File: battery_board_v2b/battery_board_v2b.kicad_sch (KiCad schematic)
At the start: 117 parts, among them IC1 PCA9685PW,118, IC2 LT3652IMSE#PBF, IC3 PCT2075DP,118, J1 Face0, J11 CHARGE, J12 Foot0, J13 Foot1, J14 Foot2, J15 Foot3, J16 RBF, J17 BURN, J18 Bypass, J19 Heater, J2 Face1, J3 Face2, J4 Face3, J5 Face4, J6 FC_FACE, J7 5V Breakout, J8 ISS Foot, K1 APAN3105, Q1 IRF7458, Q2 IRF7458, Q3 MBT2222ADW1T1, Q4 MBT2222ADW1T1, Q5 IRLML2803, Q6 NDS8434, Q7 MMBT2222AT, Q8 IRLML2803, Q9 NDS8434, U1 R5460N208AA, U2 TPS54226PWPRPWP14_2P31X2P46-L, U3 INA219AxD, U4 TCA9548APWR, U5 TPS7A4501DCQT, U6 INA219AxD, U7 1049, U8 1049

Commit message: Updated to add thermocouple driver onboard
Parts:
- added C21, C23: 0.01uF, Capacitor_SMD:C_0805_2012Metric, symbol Device:C
- added C22, C27: 0.1uF, Capacitor_SMD:C_0805_2012Metric, symbol Device:C
- added C24: 1uF, Capacitor_SMD:C_0805_2012Metric, symbol Device:C
- added C25, C26: 10uF, Capacitor_SMD:C_0805_2012Metric, symbol Device:C
- added FB1, FB2, FB3: FerriteBead, Resistor_SMD:R_0603_1608Metric, symbol Device:FerriteBead
- added J9: Thermocouple, MOLEX PICO LOCK 2 POS:MOLEX_504050-0291, symbol Connector_Generic:Conn_01x02
- added JP2: SolderJumper_2_Open, Jumper:SolderJumper-2_P1.3mm_Open_RoundedPad1.0x1.5mm, symbol Jumper:SolderJumper_2_Open
- added R46: 1-MOhm, Resistor_SMD:R_0603_1608Metric, symbol Device:R_US
- added R47, R48: 100-Ohm, Resistor_SMD:R_0603_1608Metric, symbol Device:R_US
- added R49: 1k, Resistor_SMD:R_0603_1608Metric, symbol Device:R_US
- added R50: 10k-Ohm, Resistor_SMD:R_0603_1608Metric, symbol Device:R_US
- added U10: TLVH431 DBZ SOT-23, Package_TO_SOT_SMD:SOT-23, symbol Reference_Voltage:TL431DBZ
- added U11: ADS1015IDGS, Package_SO:TSSOP-10_3x3mm_P0.5mm, symbol Analog_ADC:ADS1015IDGS
- added U9: AD8495, Package_SO:MSOP-8_3x3mm_P0.65mm, symbol Sensor_Temperature:AD8495
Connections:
- net +3V3: now also C26.2, FB1.2, FB2.2, JP2.2 (B)
- net F4_SCL: now also U11.10 (SCL)
- net F4_SDA: now also U11.9 (SDA)
- net GND: now also C21.1, C23.2, C24.2, C26.1, FB3.2, R46.2, R50.1, U10.3 (A), U9.3 (-Vs)
- new net: JP2.1 (A), R50.2, U11.1 (ADDR)
- new net: J9.1 (Pin_1), R46.1, R48.2
- new net: C24.1, FB1.1, R49.2, U9.7 (+Vs)
- new net: C21.2, C22.2, R47.2, U9.1 (-IN)
- new net: C22.1, C23.1, R48.1, U9.8 (+IN)
- new net: J9.2 (Pin_2), R47.1
- new net: R49.1, U10.1 (K), U10.2 (REF), U9.2 (REF)
- new net AGND: C25.2, C27.2, FB3.1, U11.3 (GND)
- new net AVDD: C25.1, C27.1, FB2.1, U11.4 (AIN0), U11.6 (AIN2), U11.7 (AIN3), U11.8 (VDD)
- new net OUT: U11.5 (AIN1), U9.5 (SENSE), U9.6
- no-connect marks 26 -> 27
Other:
- note added: "Default I2C: 0x48"
- note added: "Jumped I2C: 0x49"
- moved on the sheet: J11, J17, J18, J19, J5, J6, J7, J8, R45

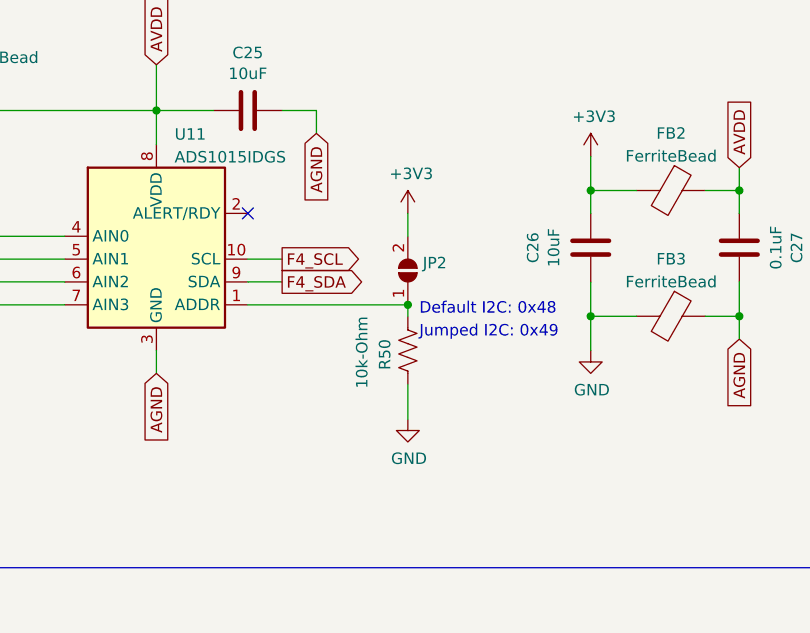
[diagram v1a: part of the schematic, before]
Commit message: Placed the thermocoupler circuitry on the board and modified schematic FOr the schematic I removed the adresse jumper ase we know which I2C adresse we are using.
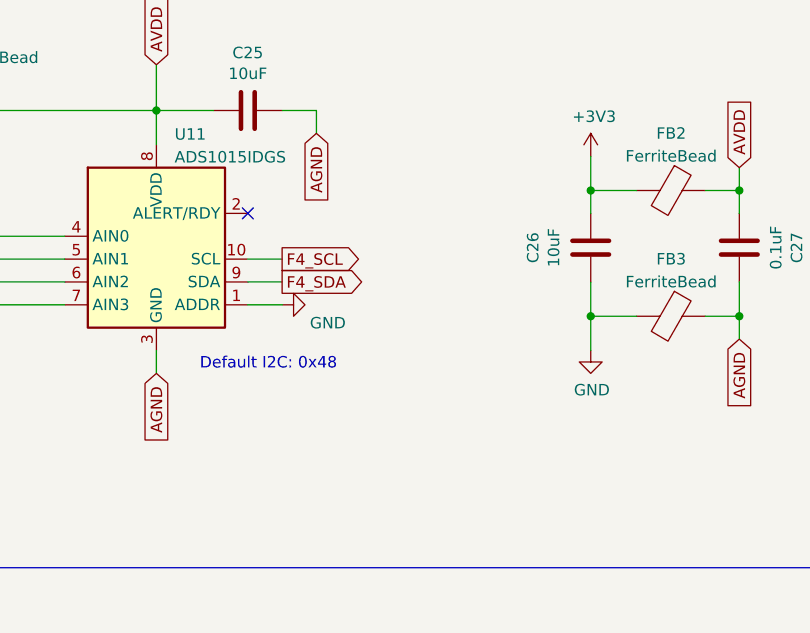
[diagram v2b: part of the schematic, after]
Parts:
- removed JP2: SolderJumper_2_Open, Jumper:SolderJumper-2_P1.3mm_Open_RoundedPad1.0x1.5mm, symbol Jumper:SolderJumper_2_Open
- removed R50: 10k-Ohm, Resistor_SMD:R_0603_1608Metric, symbol Device:R_US
- C21, C22, C23, C24, C25, C26, C27: footprint Capacitor_SMD:C_0805_2012Metric -> Capacitor_SMD:C_0402_1005Metric_Pad0.74x0.62mm_HandSolder
- R46, R47, R48, R49: footprint Resistor_SMD:R_0603_1608Metric -> Resistor_SMD:R_0402_1005Metric_Pad0.72x0.64mm_HandSolder
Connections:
- net GND: now also U11.1 (ADDR)
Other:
- note removed: "Jumped I2C: 0x49"

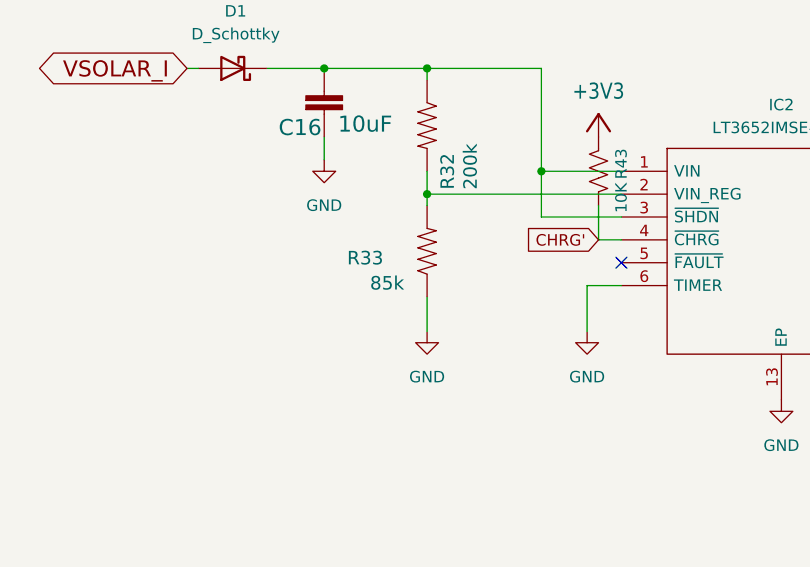
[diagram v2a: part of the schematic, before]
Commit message: Updated BOM to reflect parts availability
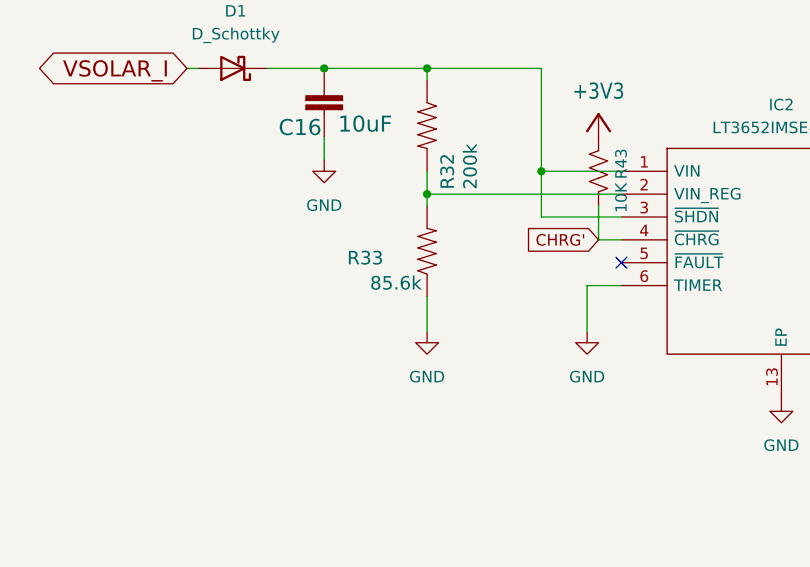
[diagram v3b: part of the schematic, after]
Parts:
- R33: value 85k -> 85.6k
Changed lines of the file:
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@@
 			)
 		)
-		(property "Value" "85k"
+		(property "Value" "85.6k"
 			(at 452.12 147.066 90)
 			(effects

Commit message: Reliability Improvements
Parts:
- removed C13, C19: 200uF, Capacitor_SMD:C_1210_3225Metric, symbol Device:C
- removed R45: 0.002, Resistor_SMD:R_2512_6332Metric, symbol mainboard:R-US_R2512
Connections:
- net B-: now also J8.2 (Pin_2)
- net GND: no longer J8.2 (Pin_2)

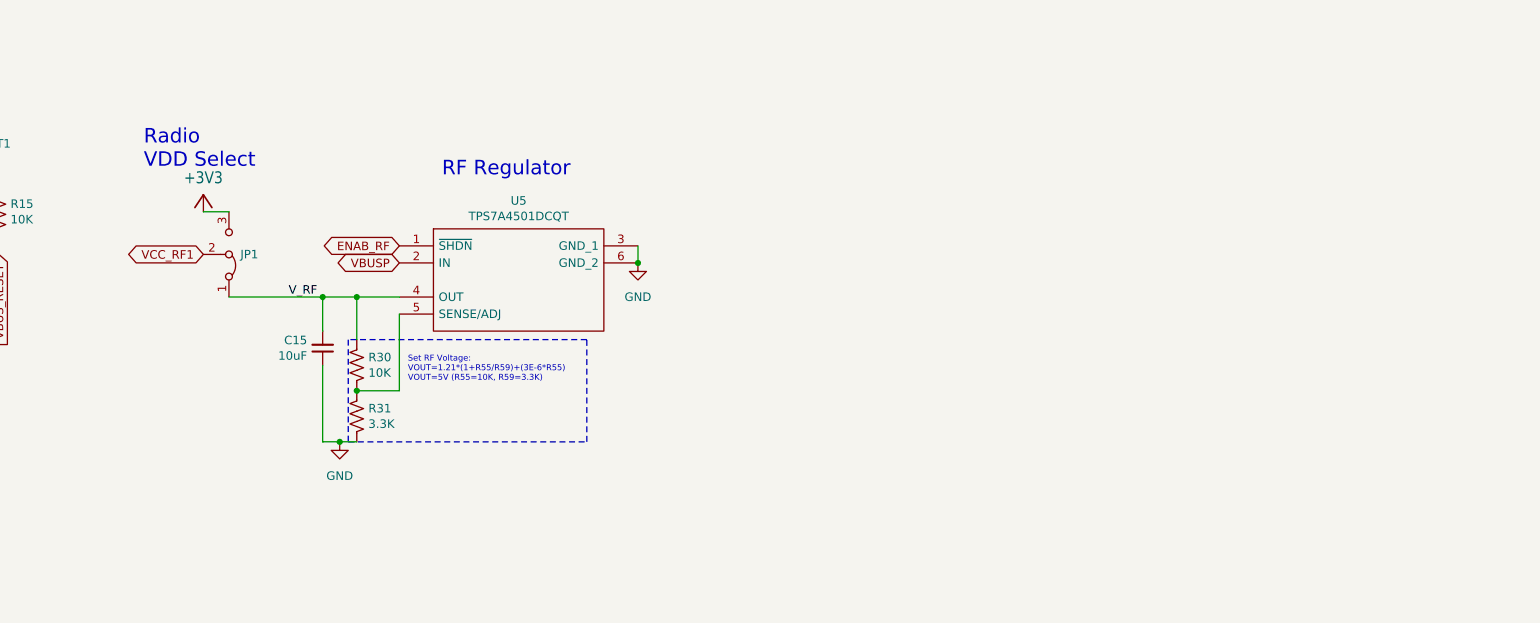
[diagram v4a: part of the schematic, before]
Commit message: Changed the 5V buck converter to a more efficient one
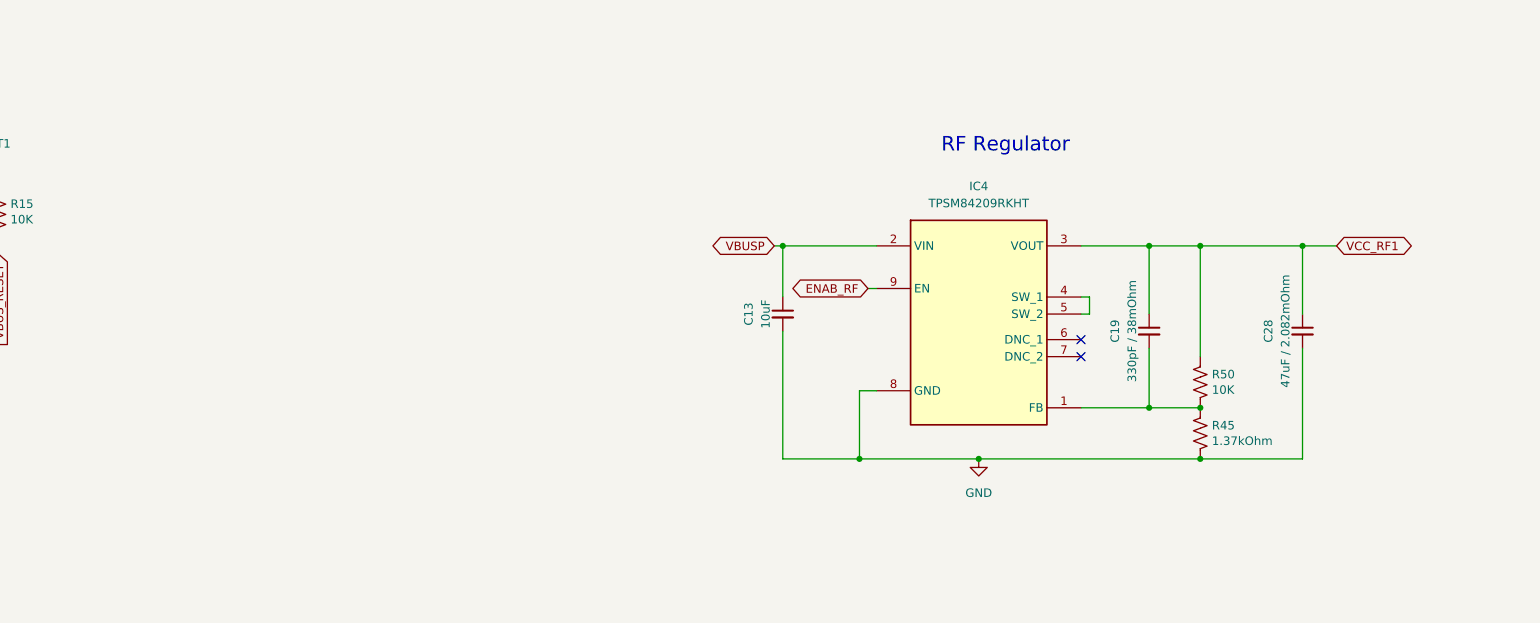
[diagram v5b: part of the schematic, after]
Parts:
- removed C15: 10uF, Capacitor_SMD:C_0603_1608Metric, symbol Device:C_Small
- removed JP1: Jumper_3_Bridged12, MaxLib:SolderJumper-3_P1.3mm_Bridged12_RoundedPad1.0x1.5mm, symbol mainboard-rescue:Jumper_3_Bridged12-Jumper
- removed R30: 10K, Resistor_SMD:R_0603_1608Metric, symbol Device:R_US
- removed R31: 3.3K, Resistor_SMD:R_0603_1608Metric, symbol Device:R_US
- removed U5: TPS7A4501DCQT, MaxLib:TPS7A4501DCQT, symbol mainboard:TPS7A4501DCQT
- added C13: 10uF, Capacitor_SMD:C_0603_1608Metric, symbol Device:C_Small
- added C19: 330pF / 38mOhm, Capacitor_SMD:C_0603_1608Metric, symbol Device:C_Small
- added C28: 47uF / 2.082mOhm, Capacitor_SMD:C_0603_1608Metric, symbol Device:C_Small
- added IC4: TPSM84209RKHT, TPSM84209RKHT, symbol Battery_Board:TPSM84209RKHT
- added R45: 1.37kOhm, Resistor_SMD:R_0603_1608Metric, symbol Device:R_US
- added R50: 10K, Resistor_SMD:R_0603_1608Metric, symbol Device:R_US
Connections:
- net ENAB_RF: now also IC4.9 (EN)
- net GND: now also C13.2, C28.2, IC4.8 (GND), R45.2
- net VBUSP: now also C13.1, IC4.2 (VIN)
- net VCC_RF1: now also C19.1, C28.1, IC4.3 (VOUT), R50.1
- new net: C19.2, IC4.1 (FB), R45.1, R50.2
- new net: IC4.4 (SW_1), IC4.5 (SW_2)
- no-connect marks 27 -> 29
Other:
- note removed: "Radio VDD Select"
- note removed: "Set RF Voltage: VOUT=1.21*(1+R55/R59)+(3E-6*R55) VOUT=5V (R55=10K, R59=3.3K)"

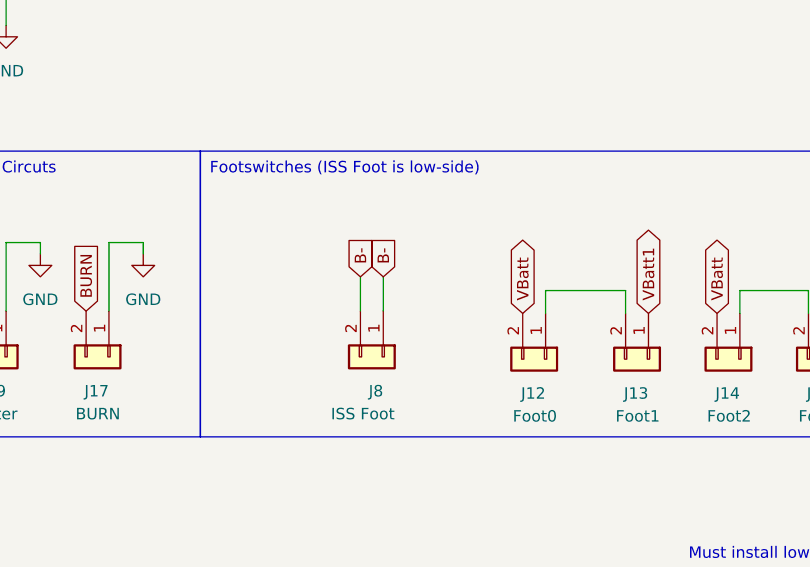
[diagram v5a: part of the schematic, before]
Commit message: Updated 5v reg and lowside switch
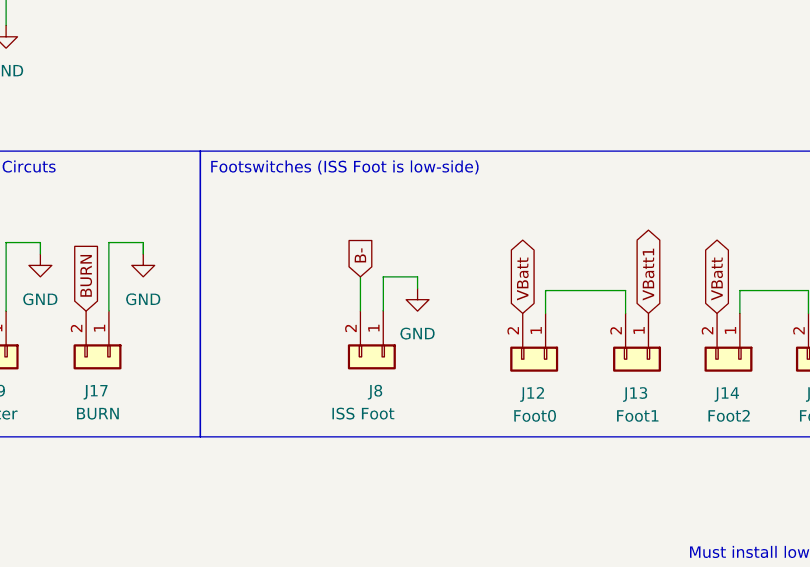
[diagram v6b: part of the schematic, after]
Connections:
- net B-: no longer J8.1 (Pin_1)
- net GND: now also J8.1 (Pin_1)
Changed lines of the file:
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@@
 	(wire
 		(pts
+			(xy 92.71 219.71) (xy 96.52 219.71)
+		)
+		(stroke
+			(width 0)
+			(type default)
+		)
+	)
+	(wire
+		(pts
 			(xy 524.51 134.62) (xy 525.78 134.62)
 		)
@@
 	(wire
 		(pts
+			(xy 96.52 219.71) (xy 96.52 220.98)
+		)
+		(stroke
+			(width 0)
+			(type default)
+		)
+	)
+	(wire
+		(pts
 			(xy 29.21 73.66) (xy 29.21 69.85)
 		)
@@
 	(label "VDD"
 		(at 90.424 332.74 0)
+		(fields_autoplaced yes)
 		(effects
 			(font
@@
 	(label "VBURN2"
 		(at 273.05 386.08 180)
+		(fields_autoplaced yes)
 		(effects
 			(font
@@
 	(label "VBURN1"
 		(at 273.05 359.41 180)
+		(fields_autoplaced yes)
 		(effects
 			(font
@@
 	(label "3V3_EN"
 		(at 123.19 48.26 0)
+		(fields_autoplaced yes)
 		(effects
 			(font
@@
 		)
 	)
-	(global_label "B-"
-		(shape input)
-		(at 92.71 219.71 90)
-		(fields_autoplaced yes)
-		(effects
-			(font
-				(size 1.27 1.27)
-			)
-			(justify left)
-		)
-		(property "Intersheetrefs" "${INTERSHEET_REFS}"
-			(at 92.71 213.8824 90)
-			(effects
-				(font
-					(size 1.27 1.27)
-				)
-				(justify left)
-				(hide yes)
-			)
-		)
-	)
 	(global_label "SDA_MAIN"
 		(shape bidirectional)
@@
 					(unit 1)
 				)
+			)
+		)
+	)
+	(symbol
+		(lib_id "power:GND")
+		(at 96.52 220.98 0)
+		(unit 1)
+		(exclude_from_sim no)
+		(in_bom yes)
+		(on_board yes)
+		(dnp no)
+		(fields_autoplaced yes)
+		(property "Reference" "#PWR015"
+			(at 96.52 227.33 0)
+			(effects
+				(font
+					(size 1.27 1.27)
+				)
+				(hide yes)
+			)
+		)
+		(property "Value" "GND"
+			(at 96.52 226.06 0)
+			(effects
+				(font
+					(size 1.27 1.27)
+				)
+			)
+		)
+		(property "Footprint" ""
+			(at 96.52 220.98 0)
+			(effects
+				(font
+					(size 1.27 1.27)
+				)
+				(hide yes)
+			)
+		)
+		(property "Datasheet" ""
+			(at 96.52 220.98 0)
+			(effects
+				(font
+					(size 1.27 1.27)
+				)
+				(hide yes)
+			)
+		)
+		(property "Description" ""
+			(at 96.52 220.98 0)
+			(effects
+				(font
+					(size 1.27 1.27)
+				)
+				(hide yes)
+			)
+		)
+		(pin "1"
+		)
+		(instances
+			(project "battery_board_v2b"
+				(path "/72946c1b-39de-434d-93c8-4c1df6a46ed0"
+					(reference "#PWR015")
+					(unit 1)
+				)
